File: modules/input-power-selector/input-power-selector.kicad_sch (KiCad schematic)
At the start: 21 parts, among them Q1 SI4909DY-T1-GE3, Q2 SI4909DY-T1-GE3, Q3 SI4909DY-T1-GE3, U1 LTC4417IGN

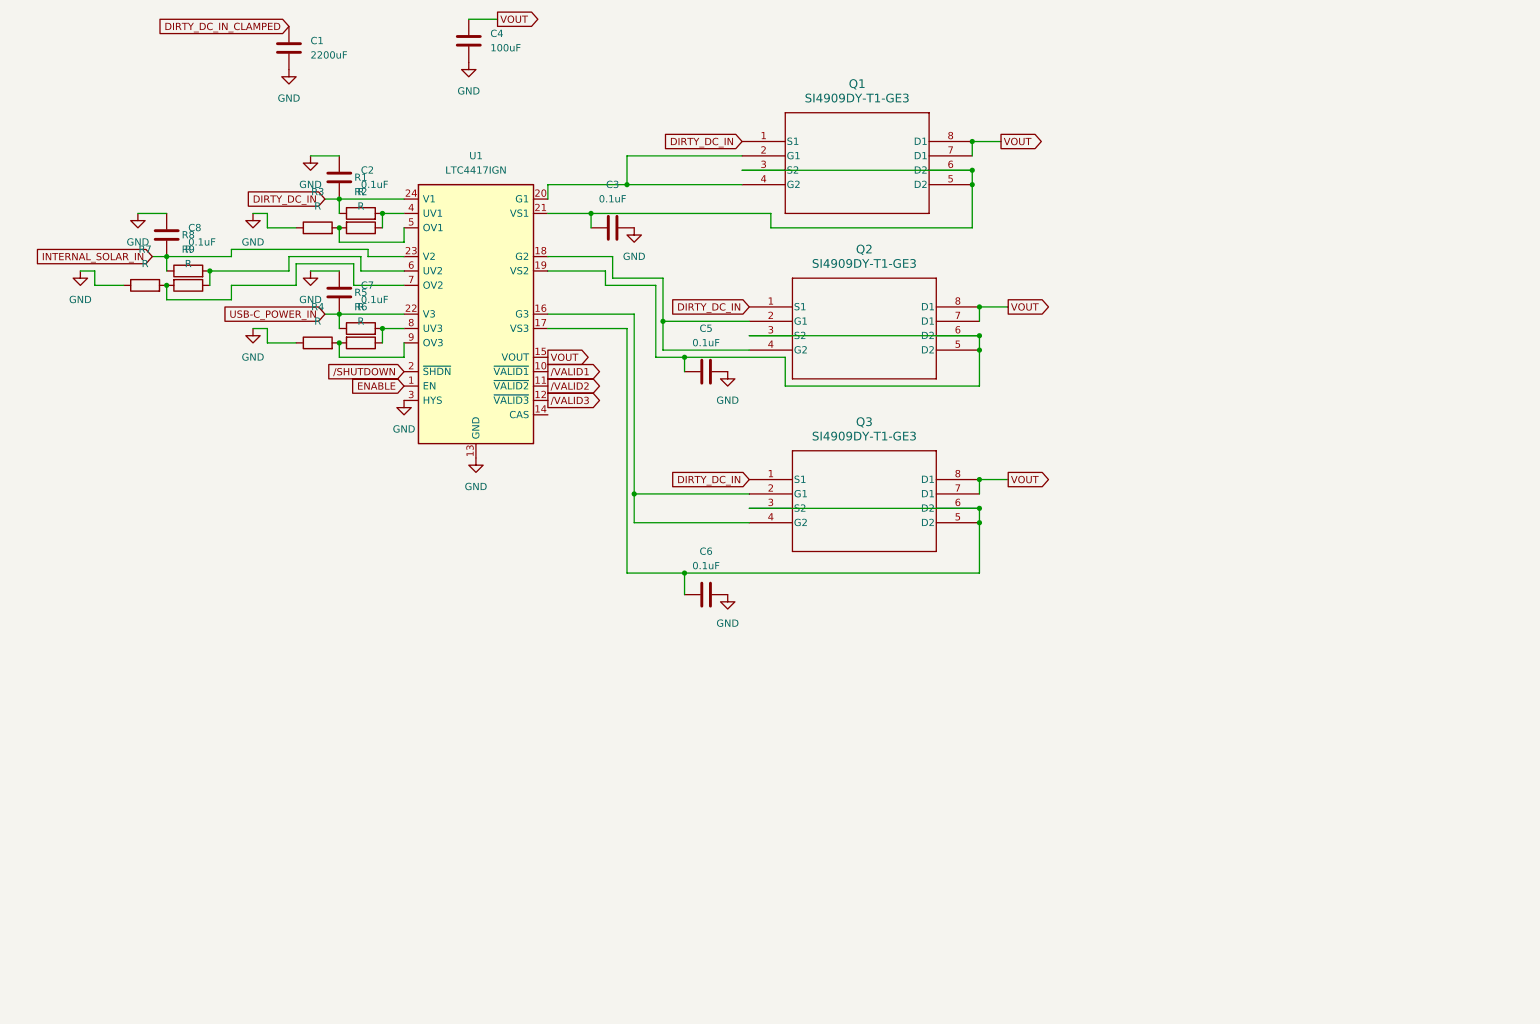
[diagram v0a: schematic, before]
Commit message: add symbols and footprints for input power selector components
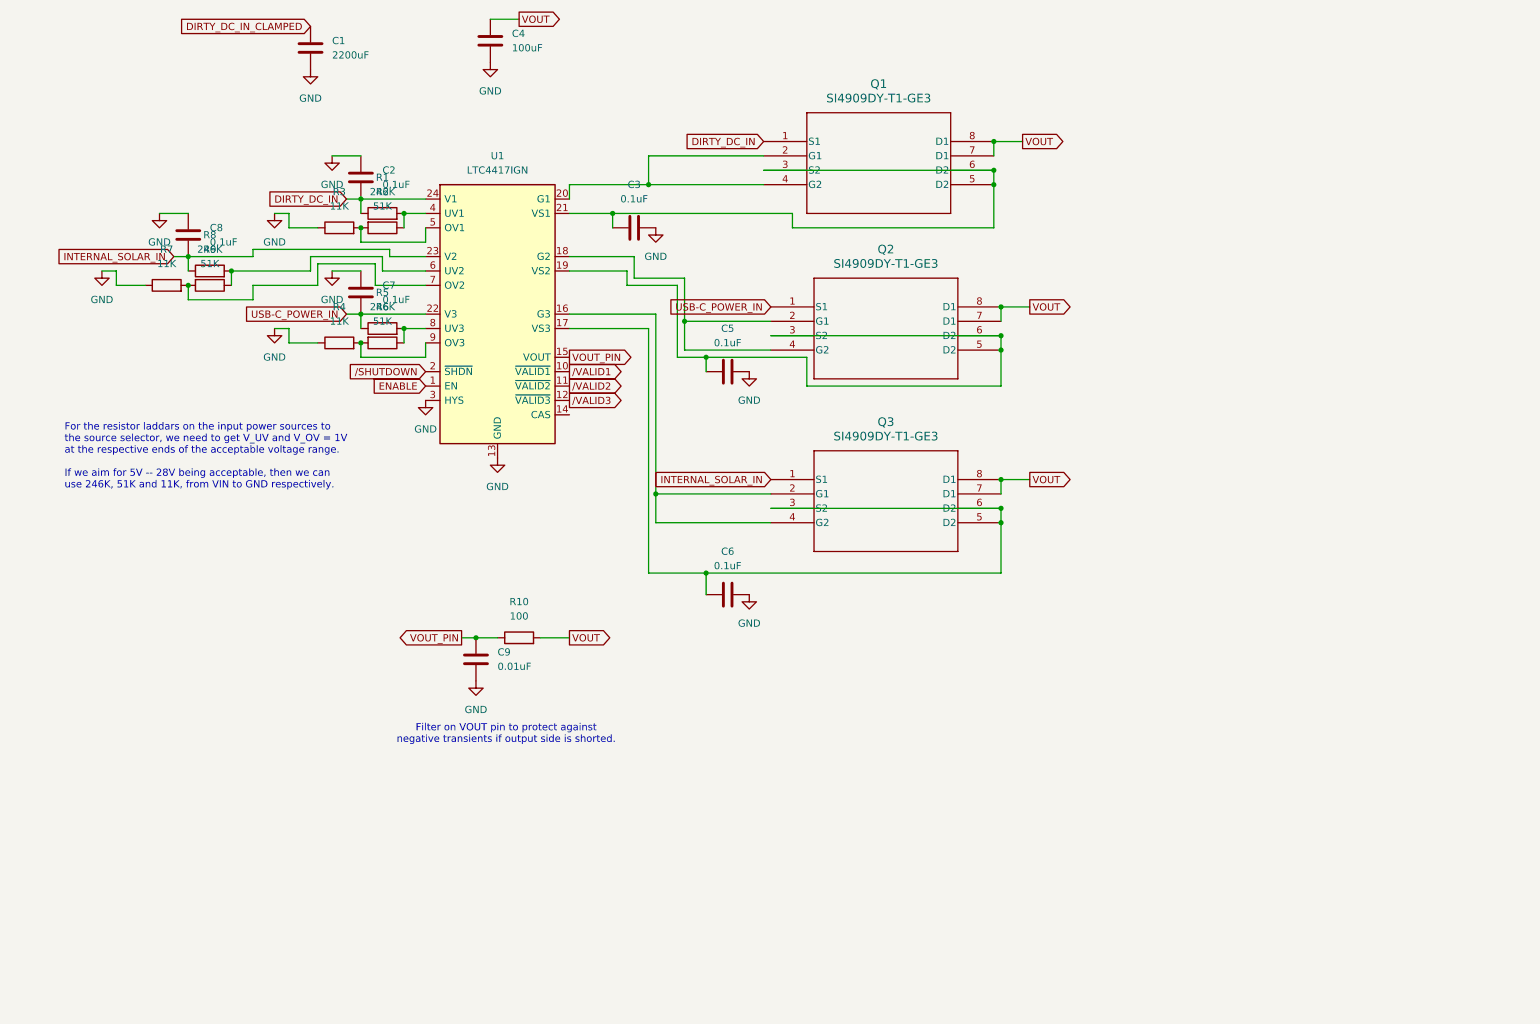
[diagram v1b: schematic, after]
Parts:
- added C9: 0.01uF, symbol Device:C
- added R10: 100, symbol Device:R
- R1, R5, R8: value R -> 246K
- R2, R6, R9: value R -> 51K
- R3, R4, R7: value R -> 11K
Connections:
- net DIRTY_DC_IN: no longer Q2.1 (S1), Q3.1 (S1)
- net GND: now also C9.2
- net INTERNAL_SOLAR_IN: now also Q3.1 (S1)
- net USB-C_POWER_IN: now also Q2.1 (S1)
- net VOUT: now also R10.2; no longer U1.15 (VOUT)
- new net VOUT_PIN: C9.1, R10.1, U1.15 (VOUT)
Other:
- note added: "Filter on VOUT pin to protect against negative transients if output side is shorted."
- note added: "For the resistor laddars on the input power sources to the source selector, we need to get V_UV and V_OV = 1V at the respective ends of the acceptable voltage range. If we aim for 5V -- 28V being acceptable, then we can use 246K, 51K and 11K, from VIN to GND respectively."
- moved on the sheet: C1, C2, C3, C4, C5, C6, C7, C8, Q1, Q2, Q3, R1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

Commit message: finish laying out schematic for power selector input protection
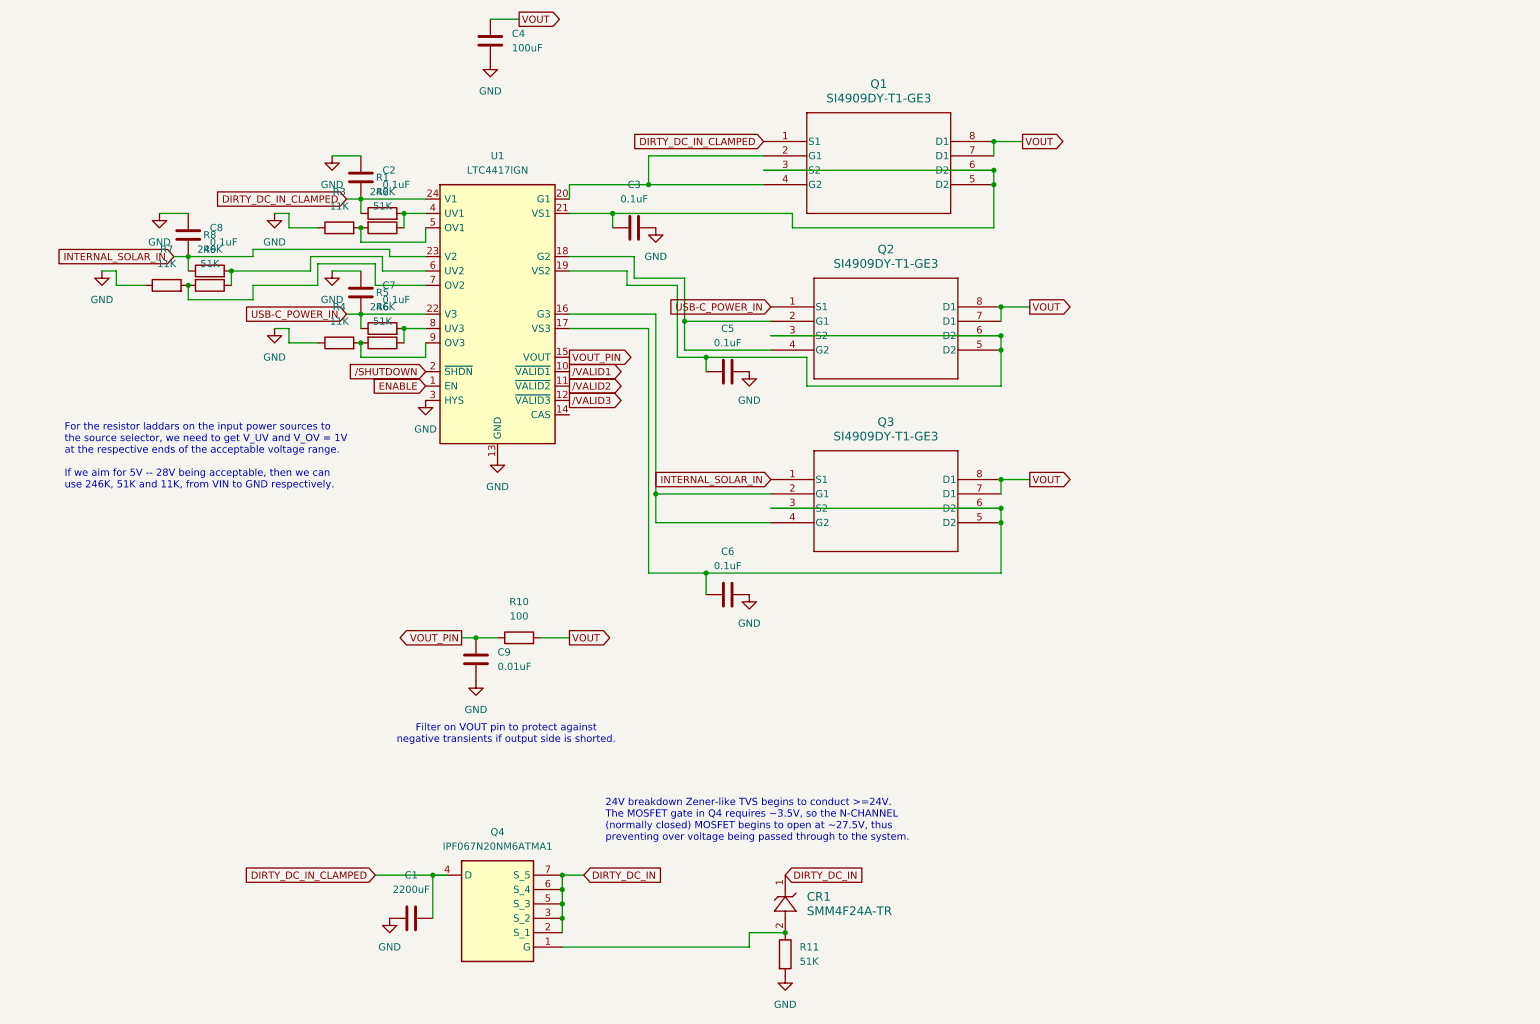
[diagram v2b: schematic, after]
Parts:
- added CR1: SMM4F24A-TR, ZDO_STMITE-FLAT_DO222-AA_STM, symbol 2025-03-01_11-33-46:SMM4F24A-TR
- added Q4: IPF067N20NM6ATMA1, IPF067N20NM6ATMA1, symbol IPF067N20NM6ATMA1:IPF067N20NM6ATMA1
- added R11: 51K, symbol Device:R
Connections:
- net DIRTY_DC_IN: now also CR1.1, Q4.2 (S_1), Q4.3 (S_2), Q4.5 (S_3), Q4.6 (S_4), Q4.7 (S_5); no longer C2.2, Q1.1 (S1), R1.1, U1.24 (V1)
- net DIRTY_DC_IN_CLAMPED: now also C1.2, C2.2, Q1.1 (S1), R1.1, U1.24 (V1), Q4.4 (D); no longer C1.1
- net GND: now also C1.1, R11.2; no longer C1.2
- new net: CR1.2, Q4.1 (G), R11.1
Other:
- note added: "24V breakdown Zener-like TVS begins to conduct >=24V. The MOSFET gate in Q4 requires ~3.5V, so the N-CHANNEL (normally closed) MOSFET begins to open at ~27.5V, thus preventing over voltage being passed through to the system."

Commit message: prepare for pcb layout for power selector
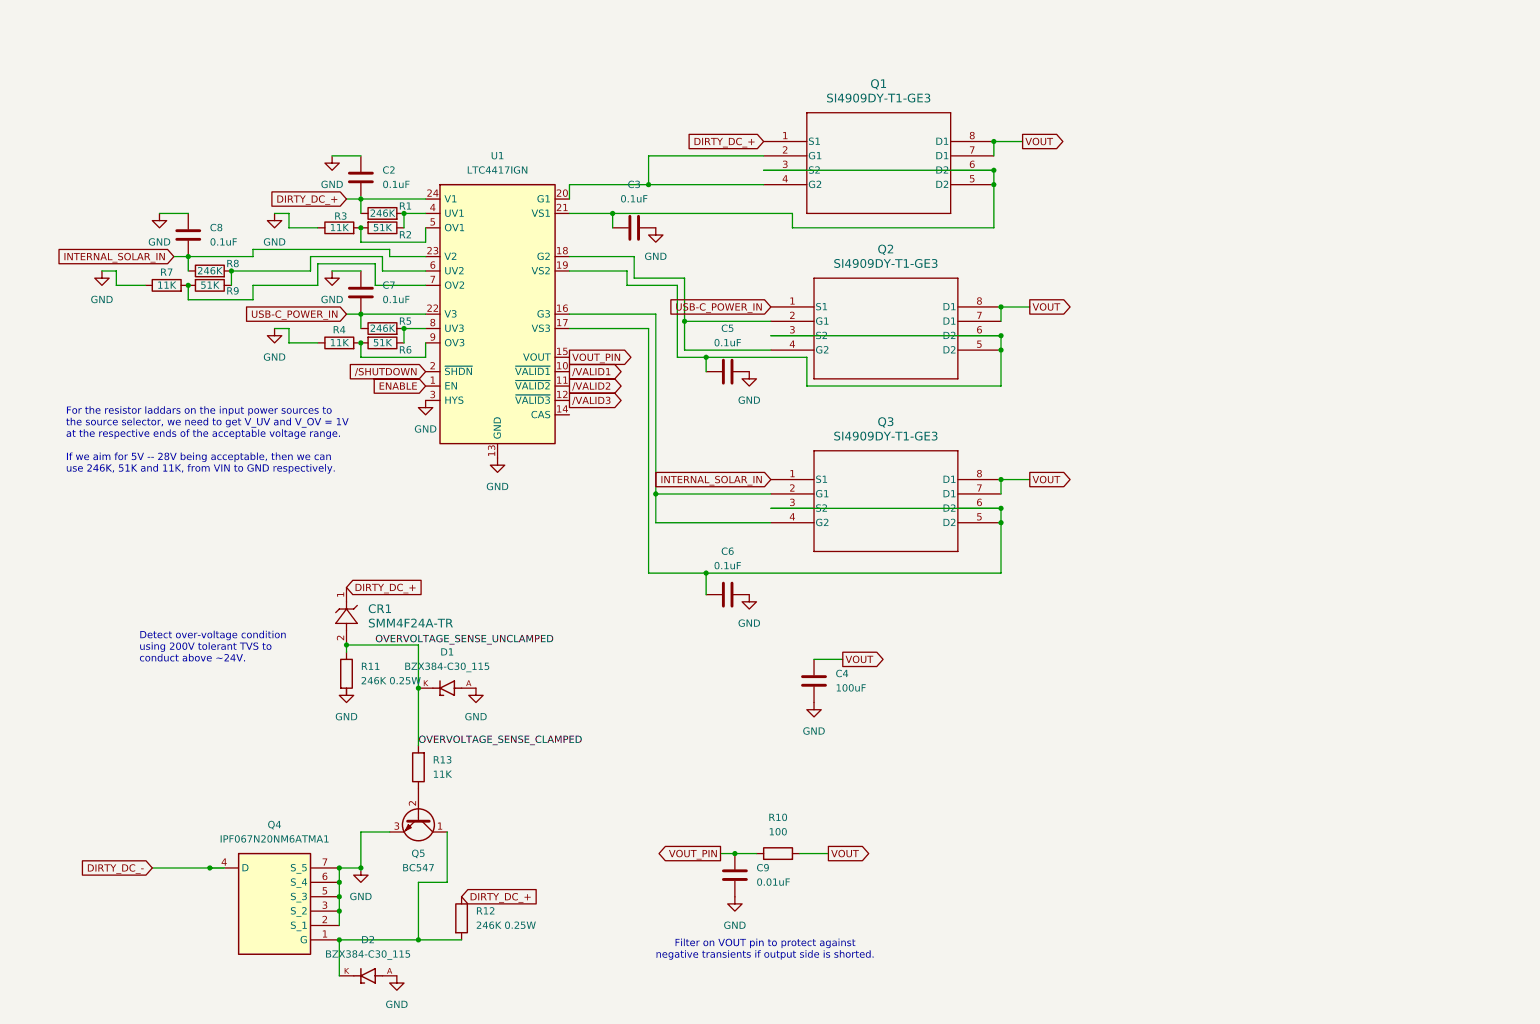
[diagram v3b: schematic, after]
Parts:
- removed C1: 2200uF, symbol Device:C
- added D1, D2: BZX384-C30_115, BZX384-C30_115:DIO_BZX384-C30_115, symbol BZX384-C30_115:BZX384-C30_115
- added Q5: BC547, Package_TO_SOT_THT:TO-92_Inline, symbol Transistor_BJT:BC547
- added R12: 246K 0.25W, Resistor_SMD:R_0805_2012Metric, symbol Device:R
- added R13: 11K, Resistor_SMD:R_0805_2012Metric, symbol Device:R
- C2, C3, C4, C5, C6, C8, C9: footprint (none) -> Capacitor_SMD:C_0805_2012Metric
- R1, R10, R2, R3, R4, R5, R6, R7, R8, R9: footprint (none) -> Resistor_SMD:R_0805_2012Metric
- R11: value 51K -> 246K 0.25W; footprint (none) -> Resistor_SMD:R_0805_2012Metric
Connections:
- net GND: now also Q4.2 (S_1), Q4.3 (S_2), Q4.5 (S_3), Q4.6 (S_4), Q4.7 (S_5), D1.A, D2.A, Q5.3 (E); no longer R11.2
- net OVERVOLTAGE_SENSE_CLAMPED: now reaches CR1.2, R11.1
- net OVERVOLTAGE_SENSE_CLAMPED: now also D1.K, R13.2; no longer Q4.1 (G)
- removed net DIRTY_DC_IN: CR1.1, Q4.2 (S_1), Q4.3 (S_2), Q4.5 (S_3), Q4.6 (S_4), Q4.7 (S_5)
- net DIRTY_DC_IN_CLAMPED renamed DIRTY_DC_+
- net DIRTY_DC_+: now also CR1.1, R12.1; no longer Q4.4 (D)
- new net: D2.K, Q4.1 (G), Q5.1 (C), R12.2
- new net: Q5.2 (B), R13.1
- new net DIRTY_DC_-: Q4.4 (D)
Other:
- note added: "Detect over-voltage condition using 200V tolerant TVS to conduct above ~24V."
- note removed: "24V breakdown Zener-like TVS begins to conduct >=24V. The MOSFET gate in Q4 requires ~3.5V, so the N-CHANNEL (normally closed) MOSFET begins to open at ~27.5V, thus preventing over voltage being passed through to the system."
- moved on the sheet: C4, C9, CR1, Q4, R10, R11

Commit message: add footprints for SMCJ28A. work on reverse polarity protection
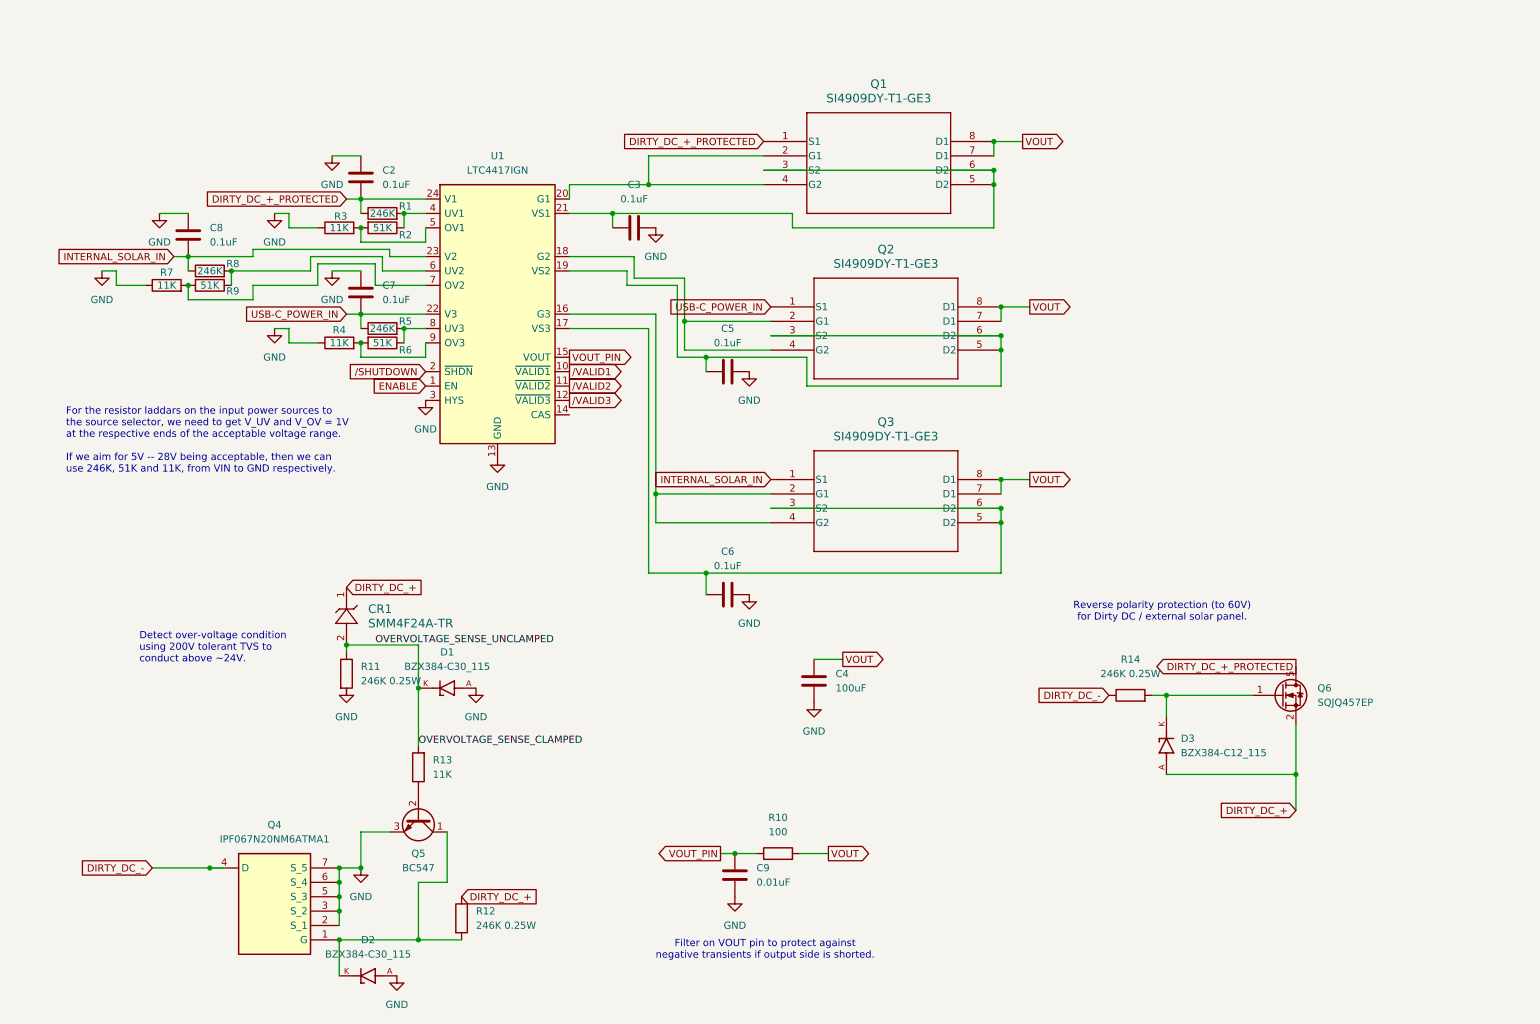
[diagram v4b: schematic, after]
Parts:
- added D3: BZX384-C12_115, BZX384-C30_115:DIO_BZX384-C30_115, symbol BZX384-C30_115:BZX384-C30_115
- added Q6: SQJQ457EP, Package_SO:PowerPAK_SO-8L_Single, symbol Transistor_FET:SQJQ466E
- added R14: 246K 0.25W, Resistor_SMD:R_0805_2012Metric, symbol Device:R
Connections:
- net DIRTY_DC_+: now also D3.A, Q6.2 (S), Q6.3 (S), Q6.4 (S); no longer C2.2, Q1.1 (S1), R1.1, U1.24 (V1)
- net DIRTY_DC_-: now also R14.1
- new net: D3.K, Q6.1 (G), R14.2
- new net DIRTY_DC_+_PROTECTED: C2.2, Q1.1 (S1), Q6.5 (D), R1.1, U1.24 (V1)
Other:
- note added: "Reverse polarity protection (to 60V) for Dirty DC / external solar panel."
